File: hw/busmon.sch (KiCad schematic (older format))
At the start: 25 parts, among them J1 CONN_01X08, J2 CONN_01X08, J3 DIL14, J4 DIL14, J5 DIL14, J6 DIL14, J7 CONN_01X02, J8 CONN_01X06, Q1 MMBT3906, Q2 MMBT3906, Q3 MMBT3906, Q4 MMBT3906, U1 ATMEGA164A-A

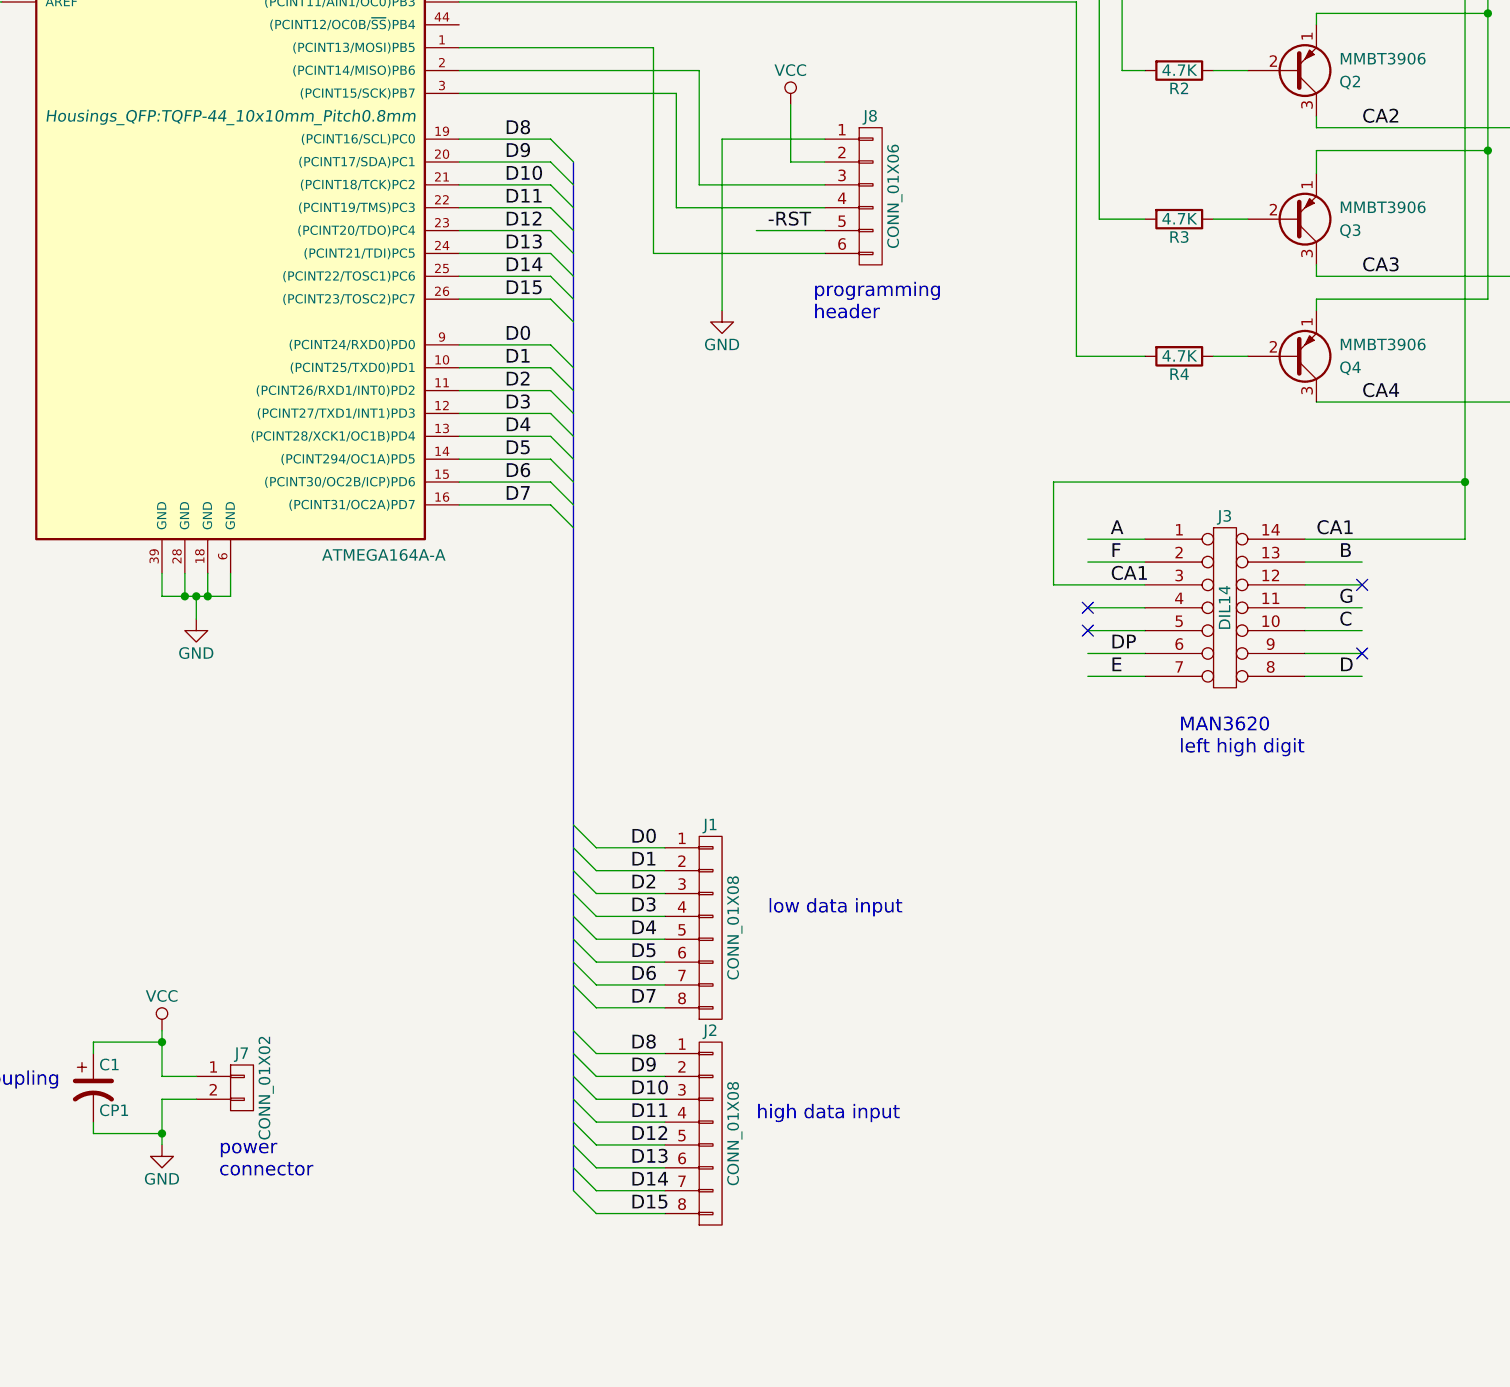
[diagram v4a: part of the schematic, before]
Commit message: use 1x16 header for data input
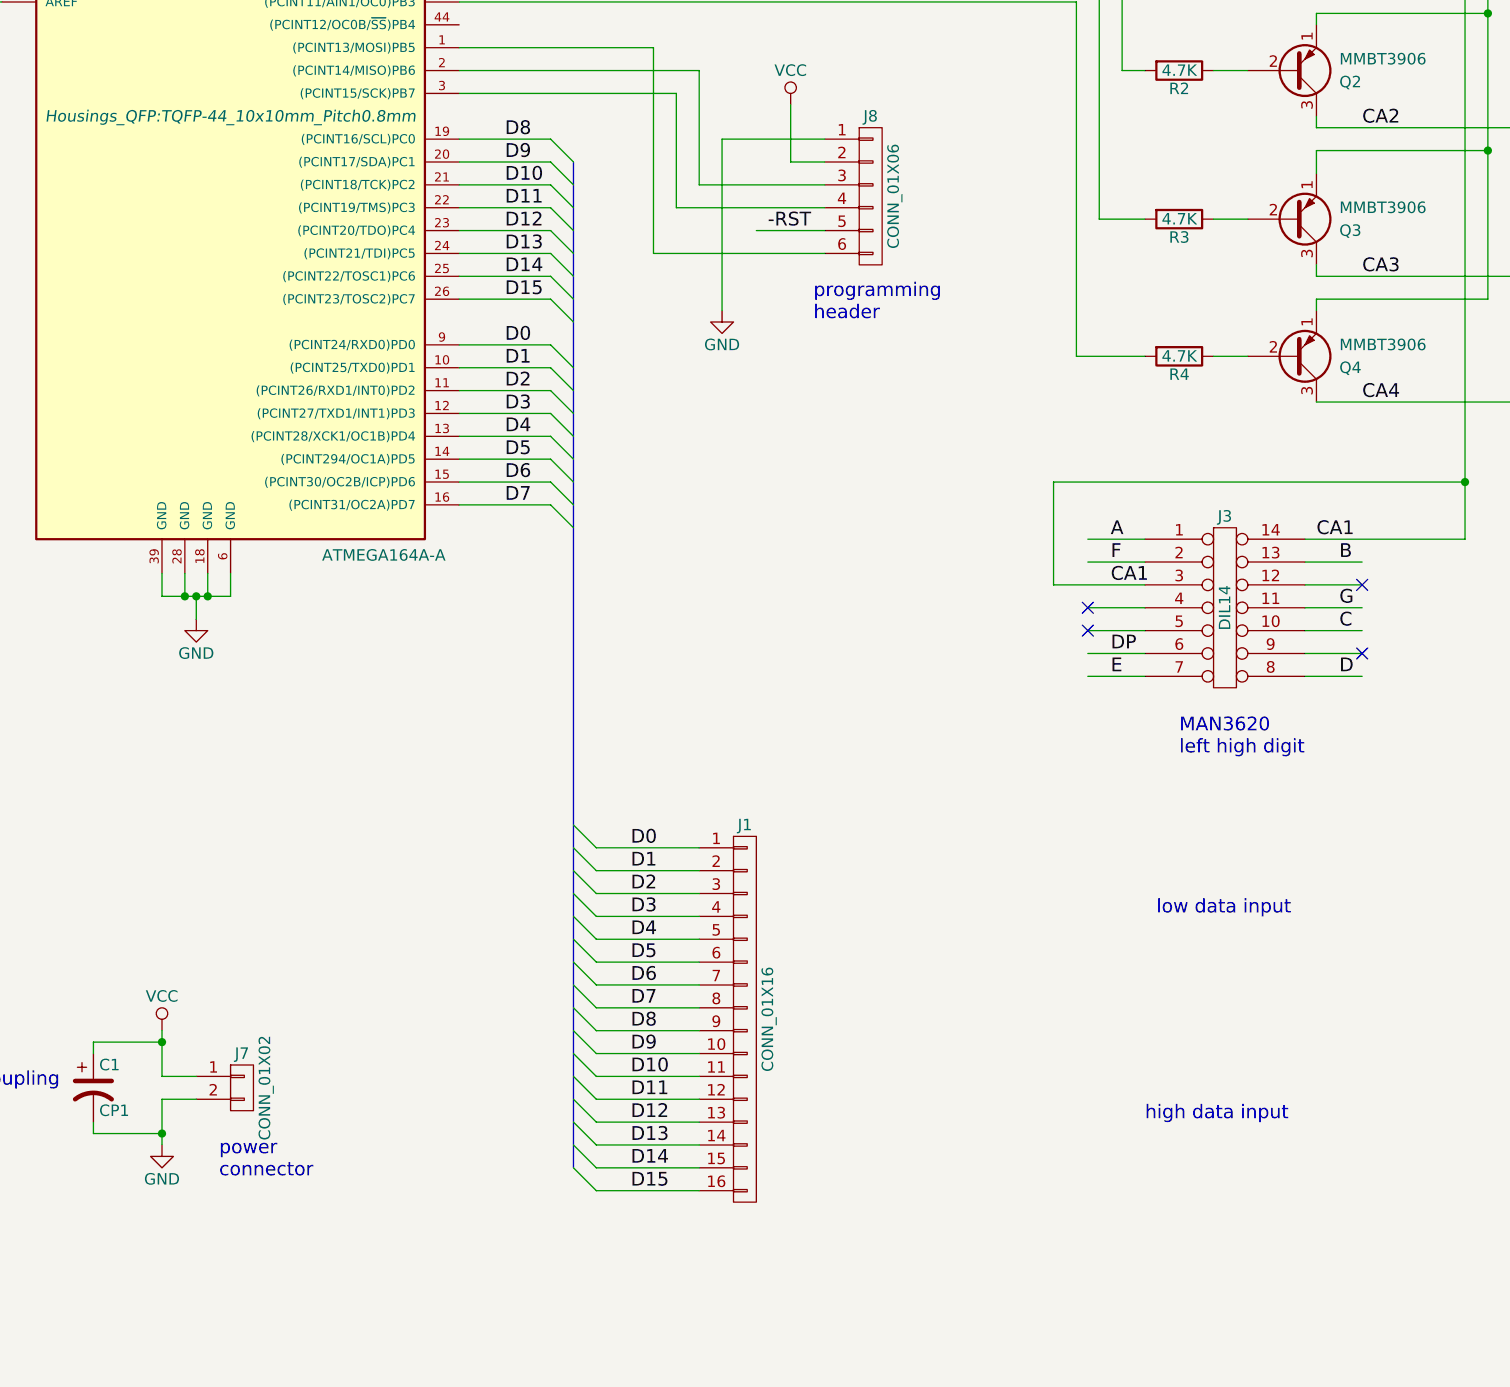
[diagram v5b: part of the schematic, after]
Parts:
- removed J1, J2: CONN_01X08, Pin_Headers:Pin_Header_Straight_1x08_Pitch2.54mm, symbol CONN_01X08
- added J1: CONN_01X16, Pin_Headers:Pin_Header_Straight_1x16_Pitch2.54mm, symbol CONN_01X16
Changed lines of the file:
@@
 CA2
-$Comp
-L CONN_01X08 J1
-U 1 1 592DF998
-P 5400 7800
-F 0 "J1" H 5400 8250 50  0000 C CNN
-F 1 "CONN_01X08" V 5500 7800 50  0000 C CNN
-F 2 "Pin_Headers:Pin_Header_Straight_1x08_Pitch2.54mm" H 5400 7800 50  0001 C CNN
-F 3 "" H 5400 7800 50  0001 C CNN
-	1    5400 7800
-	1    0    0    -1
-$EndComp
 $Comp
 L Q_PNP_EBC Q1
@@
 	4300 3150 4650 3150
 Wire Wire Line
-	4900 7450 5200 7450
-Wire Wire Line
-	4900 7550 5200 7550
-Wire Wire Line
-	4900 7650 5200 7650
-Wire Wire Line
-	4900 7750 5200 7750
-Wire Wire Line
-	4900 7850 5200 7850
-Wire Wire Line
-	4900 7950 5200 7950
-Wire Wire Line
-	4900 8050 5200 8050
-Wire Wire Line
-	4900 8150 5200 8150
+	4900 7450 5350 7450
+Wire Wire Line
+	4900 7550 5350 7550
+Wire Wire Line
+	4900 7650 5350 7650
+Wire Wire Line
+	4900 7750 5350 7750
+Wire Wire Line
+	4900 7850 5350 7850
+Wire Wire Line
+	4900 7950 5350 7950
+Wire Wire Line
+	4900 8050 5350 8050
+Wire Wire Line
+	4900 8150 5350 8150
 Wire Wire Line
 	8050 3250 8050 3200
@@
 $EndComp
 Wire Wire Line
-	3150 8450 3000 8450
-Wire Wire Line
-	3000 8450 3000 8250
+	3000 8450 3150 8450
+Wire Wire Line
+	3000 8250 3000 8450
 Wire Wire Line
 	3150 8550 3000 8550
@@
 Text Notes 3250 8900 0    60   ~ 0
 power\nconnector
-Text Notes 5650 7750 0    60   ~ 0
+Text Notes 7350 7750 0    60   ~ 0
 low data input
 $Comp
@@
 Text Notes 13650 7050 0    60   ~ 0
 MAN3620\nright low digit
-$Comp
-L CONN_01X08 J2
-U 1 1 593E763B
-P 5400 8700
-F 0 "J2" H 5400 9150 50  0000 C CNN
-F 1 "CONN_01X08" V 5500 8700 50  0000 C CNN
-F 2 "Pin_Headers:Pin_Header_Straight_1x08_Pitch2.54mm" H 5400 8700 50  0001 C CNN
-F 3 "" H 5400 8700 50  0000 C CNN
-	1    5400 8700
-	1    0    0    -1
-$EndComp
 Wire Wire Line
 	3000 6250 3000 6350
@@
 D15
 Wire Bus Line
-	4800 4450 4800 8950
+	4800 4450 4800 8850
 Entry Wire Line
 	4700 4350 4800 4450
@@
 	4700 5950 4800 6050
 Wire Wire Line
-	5200 8350 4900 8350
-Wire Wire Line
-	5200 8450 4900 8450
-Wire Wire Line
-	5200 8550 4900 8550
-Wire Wire Line
-	5200 8650 4900 8650
-Wire Wire Line
-	5200 8750 4900 8750
-Wire Wire Line
-	5200 8850 4900 8850
-Wire Wire Line
-	5200 8950 4900 8950
-Wire Wire Line
-	5200 9050 4900 9050
+	5350 8250 4900 8250
+Wire Wire Line
+	5350 8350 4900 8350
+Wire Wire Line
+	5350 8450 4900 8450
+Wire Wire Line
+	5350 8550 4900 8550
+Wire Wire Line
+	5350 8650 4900 8650
+Wire Wire Line
+	5350 8750 4900 8750
+Wire Wire Line
+	5350 8850 4900 8850
+Wire Wire Line
+	5350 8950 4900 8950
 Text Label 5050 7450 0    60   ~ 0
 D0
@@
 Text Label 5050 8150 0    60   ~ 0
 D7
-Text Notes 5600 8650 0    60   ~ 0
+Text Notes 7300 8650 0    60   ~ 0
 high data input
+Text Label 5050 8250 0    60   ~ 0
+D8
 Text Label 5050 8350 0    60   ~ 0
-D8
+D9
 Text Label 5050 8450 0    60   ~ 0
-D9
+D10
 Text Label 5050 8550 0    60   ~ 0
-D10
+D11
 Text Label 5050 8650 0    60   ~ 0
-D11
+D12
 Text Label 5050 8750 0    60   ~ 0
-D12
+D13
 Text Label 5050 8850 0    60   ~ 0
-D13
+D14
 Text Label 5050 8950 0    60   ~ 0
-D14
-Text Label 5050 9050 0    60   ~ 0
 D15
 Entry Wire Line
@@
 	4800 8050 4900 8150
 Entry Wire Line
+	4800 8150 4900 8250
+Entry Wire Line
 	4800 8250 4900 8350
 Entry Wire Line
@@
 Entry Wire Line
 	4800 8850 4900 8950
-Entry Wire Line
-	4800 8950 4900 9050
 $Comp
 L Q_PNP_EBC Q3
@@
 Text Notes 5850 5150 0    60   ~ 0
 programming\nheader
+$Comp
+L CONN_01X16 J1
+U 1 1 593ECF2F
+P 5550 8200
+F 0 "J1" H 5550 9050 50  0000 C CNN
+F 1 "CONN_01X16" V 5650 8200 50  0000 C CNN
+F 2 "Pin_Headers:Pin_Header_Straight_1x16_Pitch2.54mm" H 5550 8200 50  0001 C CNN
+F 3 "" H 5550 8200 50  0001 C CNN
+	1    5550 8200
+	1    0    0    -1
+$EndComp
 $EndSCHEMATC
